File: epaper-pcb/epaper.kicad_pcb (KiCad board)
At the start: 2 copper layers, 65 x 30 mm, 52 parts, among them J1 download, J2 epaper, J3 USB_C_Receptacle_USB2.0, J4 BATT, J5 Speaker, J6 JTAG, Q1 DMG3404L, Q2 AO3401A, Q3 S8050, Q4 S8050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

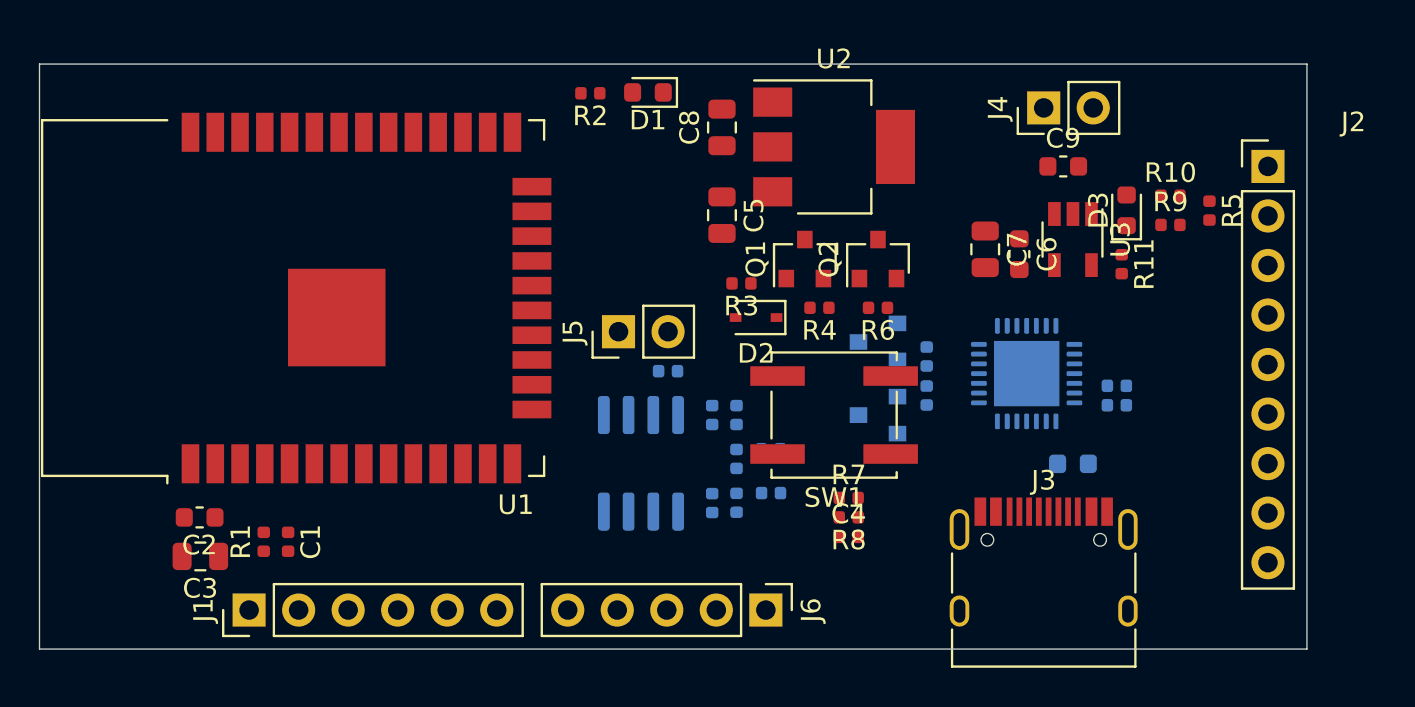
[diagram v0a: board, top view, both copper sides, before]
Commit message: feat(pcb): add pcb line design
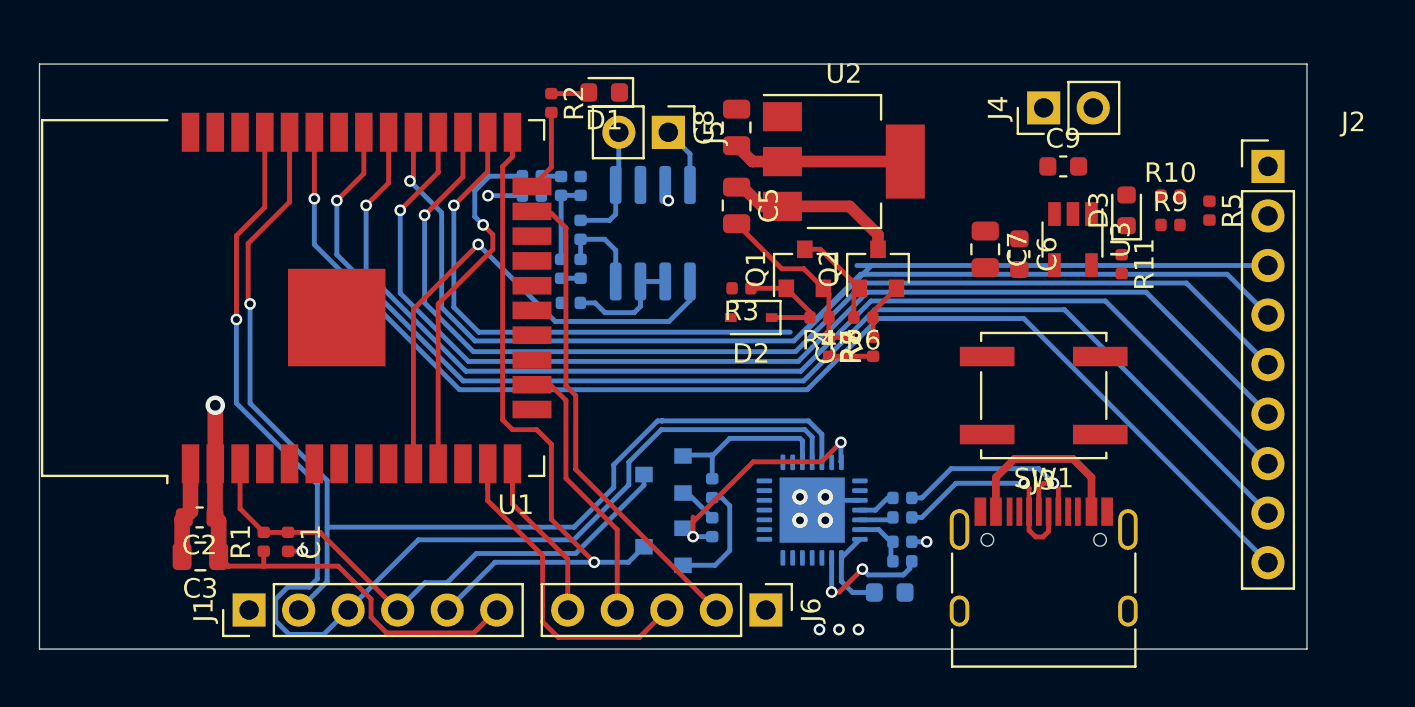
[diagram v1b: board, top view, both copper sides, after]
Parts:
- added R19: 22, Resistor_SMD:R_0402_1005Metric, B.Cu at (114.2, 113.2)
- added R20: 22, Resistor_SMD:R_0402_1005Metric, B.Cu at (114.2, 112.2)
- moved R12 19.8 mm to (95.2, 95.8), turned to 180 degrees
- moved C10 19.6 mm to (95.2, 96.8), turned to 0 degrees
- moved C11 16.7 mm to (97.8, 96.2), turned to 270 degrees
- moved R13 16.6 mm to (96.8, 96.2), turned to 90 degrees
- moved R15 15.6 mm to (97.8, 98.5), turned to 270 degrees
- moved C15 13.6 mm to (114.2, 114.5)
- moved R16 13.6 mm to (114.2, 115.5)
- moved U5 13.0 mm to (109.6, 112.9)
- moved Q3 12.9 mm to (102.0, 111.0)
- moved Q4 12.9 mm to (102.0, 114.8)
- moved R17 12.9 mm to (104.5, 113.8)
- moved R18 12.9 mm to (104.5, 111.8)
- moved U4 11.8 mm to (101.5, 98.7), turned to 90 degrees
- moved C12 11.7 mm to (96.8, 100.5), turned to 90 degrees
- moved C14 11.5 mm to (113.6, 117.1)
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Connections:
- J1 pad 4: /BOOT -> /EN
- J1 pad 5: /EN -> /BOOT
- J3 pad B6: Net-(J3-PadB6) -> Net-(J3-PadA6)
- J3 pad B7: Net-(J3-PadB7) -> Net-(J3-PadA7)
- U5 pad 4: Net-(J3-PadA6) -> Net-(R20-Pad1)
- U5 pad 5: Net-(J3-PadB6) -> Net-(R19-Pad1)
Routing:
- net /CS: track 0.00 -> 64.4 mm, vias 0 -> 1
- net /TXD0: track 0.00 -> 63.2 mm, vias 0 -> 1
- net /SCLK: track 0.00 -> 63.1 mm, vias 0 -> 1
- net /MOSI: track 0.00 -> 60.9 mm, vias 0 -> 1
- net /BUSY: track 0.00 -> 59.1 mm, vias 0 -> 1
- net /RXD0: track 0.00 -> 57.8 mm, vias 0 -> 1
- net /DC: track 0.00 -> 57.0 mm, vias 0 -> 1
- net /RESET: track 0.00 -> 55.1 mm, vias 0 -> 1
- net /POWER: track 0.00 -> 53.4 mm, vias 0 -> 1
- net /BOOT: track 0.00 -> 36.4 mm, vias 0 -> 1
- net +3V3: track 0.00 -> 34.5 mm, vias 0 -> 1
- net /EN: track 0.00 -> 28.4 mm
- net /Sheet5F555EA7/SHUTDOWN: track 0.00 -> 26.5 mm, vias 0 -> 1
- net /TDO: track 0.00 -> 23.9 mm
- net GND: track 0.00 -> 20.3 mm, vias 0 -> 11
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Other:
- net class Default: via_dia 0.8 -> 0.6; via_drill 0.4 -> 0.35
- board text added: "3V3"
- board text added: "BUSY"
- board text added: "CS"
- board text added: "D/C"
- board text added: "GND"
- board text added: "MOSI"
- board text added: "POWER"
- board text added: "RESET"
- board text added: "SCLK"

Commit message: feat(pcb): compeleted pcb line design
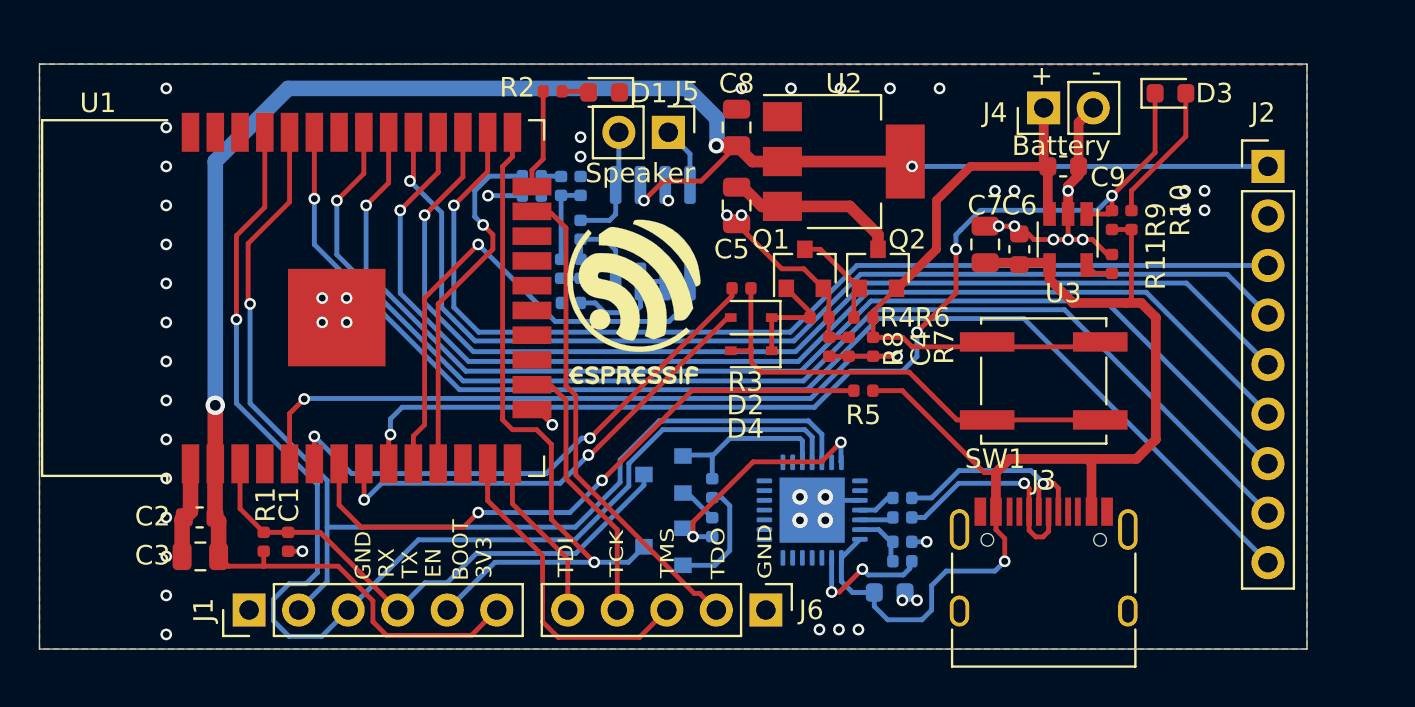
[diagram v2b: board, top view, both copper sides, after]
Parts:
- added D4: 1N4148WS, Diode_SMD:D_SOD-323, F.Cu at (106.5, 104.7)
- added G***: LOGO, epaper-pcb:espressif_logo, F.Cu at (100.5, 102.2)
- R16: value 3K -> 10K
- R3, R5: value 3K -> 4.7K
- R4: value 20K -> 10K
- moved R5 20.0 mm to (112.2, 106.8), turned to 0 degrees
- moved D3 6.41 mm to (128.0, 91.5), turned to 0 degrees
- moved R9 3.01 mm to (125.0, 98.0), turned to 270 degrees
- moved R10 2.36 mm to (126.0, 98.0), turned to 270 degrees
- moved SW1 0.75 mm to (121.5, 106.2), turned to 180 degrees
- moved R2 0.60 mm to (96.3, 91.4), turned to 180 degrees
- moved R11 0.50 mm to (125.0, 100.2)
- moved C6 0.25 mm to (120.2, 99.5)
- moved C7 0.25 mm to (118.5, 99.2)
- moved U3 0.25 mm to (122.8, 99.0)
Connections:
- R3 pad 1: Net-(D2-Pad1) -> Net-(D4-Pad2)
- SW1 pad 1: Net-(D2-Pad1) -> Net-(D4-Pad2)
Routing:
- net +3V3: track 34.5 -> 101.7 mm, vias 1 -> 4
- net /Sheet5F4ECFED/CHRG_STATE: track 0.00 -> 54.9 mm, vias 0 -> 4
- net +5V: track 13.7 -> 60.1 mm, vias 0 -> 1
- net /ADC_VOL: track 2.25 -> 38.4 mm, vias 0 -> 2
- net /Sheet5F4ECFED/USB_CHECK: track 0.00 -> 31.9 mm, vias 0 -> 2
- net +BATT: track 3.02 -> 32.7 mm
- net /Sheet5F4ECFED/BUTTON: track 0.00 -> 27.8 mm, vias 0 -> 2
- net /Sheet5F4ECFED/ENABLE: track 0.00 -> 24.6 mm, vias 0 -> 2
- net Net-(D4-Pad2): track 0.00 -> 24.0 mm
- net GND: track 20.3 -> 36.2 mm, vias 11 -> 54
- net Net-(D3-Pad2): track 0.00 -> 7.17 mm
- net Net-(R11-Pad2): track 0.00 -> 1.48 mm
- net Net-(R2-Pad2): track 4.21 -> 5.12 mm
- net Net-(J3-PadA6): track 11.8 -> 11.2 mm
- net Net-(D1-Pad2): track 1.94 -> 1.39 mm
- added copper zone on B.Cu, net GND
- added copper zone on F.Cu, net GND
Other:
- board text added: "+"
- board text added: "-"
- board text added: "BOOT"
- board text added: "Battery"
- board text added: "EN"
- board text added: "RX"
- board text added: "Speaker"
- board text added: "TCK"
- board text added: "TDI"
- board text added: "TDO"
- board text added: "TMS"
- board text added: "TX"
- board text added: "https://github.com/TDA-2030/E-ink-screen"
